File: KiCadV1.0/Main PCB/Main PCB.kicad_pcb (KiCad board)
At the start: 2 copper layers, 79 x 74 mm, 7 parts, among them J1 Conn_01x01_Male, J2 Conn_01x01_Male, U1 TM1637, U2 TM1637, U3 TM1637, U4 NEO6M

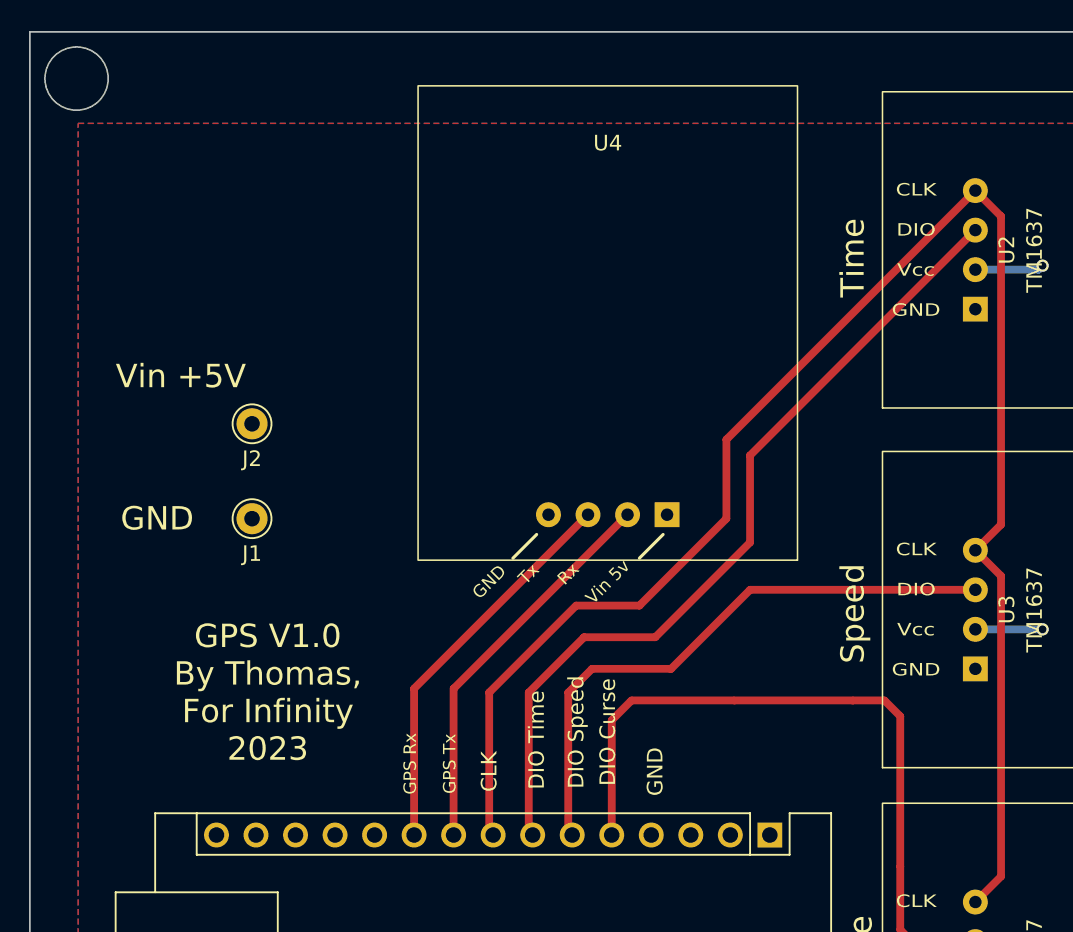
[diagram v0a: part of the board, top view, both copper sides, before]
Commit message: PCB modifs visuelles + Commande
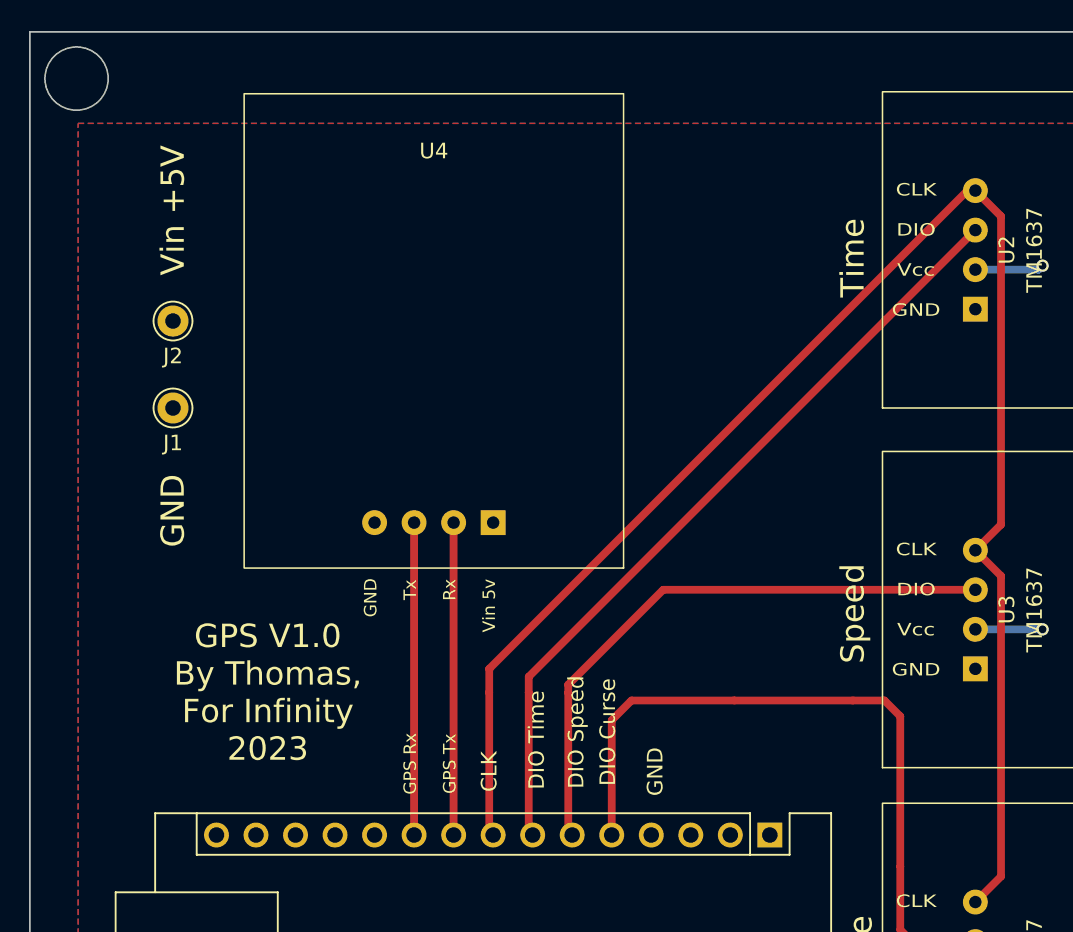
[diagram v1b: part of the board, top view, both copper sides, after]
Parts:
- moved U4 11.2 mm to (61.0, 78.7)
- moved J1 8.74 mm to (44.2, 74.2)
- moved J2 8.33 mm to (44.2, 68.6)
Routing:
- net Net-(U4-Pad2): track 25.2 -> 20.1 mm
- net Net-(U4-Pad3): track 25.2 -> 20.1 mm
- net Net-(A1-Pad7): track 53.5 -> 50.9 mm
- net Net-(U1-Pad4): track 105.3 -> 103.2 mm
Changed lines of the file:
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@@
   )
   (footprint "thomas footprint:NEO6M" (layer "F.Cu")
-    (at 72.136 78.232)
+    (at 60.96 78.74)
     (descr "8-lead though-hole mounted DIP package, row spacing 7.62 mm (300 mils), missing pin 7")
     (tags "THT DIP DIL PDIP 2.54mm 7.62mm 300mil")
@@
   )
   (footprint "Connector_Pin:Pin_D1.0mm_L10.0mm" (layer "F.Cu")
-    (at 49.276 75.184)
+    (at 44.196 68.58)
     (descr "solder Pin_ diameter 1.0mm, hole diameter 1.0mm (press fit), length 10.0mm")
     (tags "solder Pin_ press fit")
@@
   )
   (footprint "Connector_Pin:Pin_D1.0mm_L10.0mm" (layer "F.Cu")
-    (at 49.276 81.28)
+    (at 44.196 74.168)
     (descr "solder Pin_ diameter 1.0mm, hole diameter 1.0mm (press fit), length 10.0mm")
     (tags "solder Pin_ press fit")
@@
   (gr_line (start 111 121) (end 38 121) (layer "F.Paste") (width 0.1))
   (gr_line (start 38 53) (end 111 53) (layer "F.Paste") (width 0.1))
-  (gr_line (start 75.692 82.296) (end 74.168 83.82) (layer "F.SilkS") (width 0.2))
-  (gr_line (start 67.564 82.296) (end 66.04 83.82) (layer "F.SilkS") (width 0.2))
   (gr_circle (center 38 53) (end 40.032 53) (layer "Edge.Cuts") (width 0.1) (fill none))
   (gr_circle (center 111 53) (end 113.032 53) (layer "Edge.Cuts") (width 0.1) (fill none))
@@
     (effects (font (size 1 1) (thickness 0.15)))
   )
-  (gr_text "Vin 5v" (at 72.136 85.344 45) (layer "F.SilkS")
+  (gr_text "Vin 5v" (at 64.516 86.868 90) (layer "F.SilkS")
     (effects (font (size 0.8 0.8) (thickness 0.125)))
   )
@@
     (effects (font (size 1 1) (thickness 0.15)))
   )
-  (gr_text "Vin +5V" (at 44.704 72.136) (layer "F.SilkS")
-    (effects (font (size 1.5 1.5) (thickness 0.3)))
-  )
-  (gr_text "GND" (at 64.516 85.344 45) (layer "F.SilkS")
+  (gr_text "Vin +5V" (at 44.196 61.468 90) (layer "F.SilkS")
+    (effects (font (size 1.5 1.5) (thickness 0.3)))
+  )
+  (gr_text "GND" (at 56.896 86.36 90) (layer "F.SilkS")
     (effects (font (size 0.8 0.8) (thickness 0.125)))
   )
@@
     (effects (font (size 1 1) (thickness 0.15)))
   )
-  (gr_text "Rx" (at 69.596 84.836 45) (layer "F.SilkS")
+  (gr_text "Rx" (at 61.976 85.852 90) (layer "F.SilkS")
     (effects (font (size 0.8 0.8) (thickness 0.125)))
   )
@@
     (effects (font (size 1 1) (thickness 0.15)))
   )
-  (gr_text "GND" (at 43.18 81.28) (layer "F.SilkS")
+  (gr_text "GND" (at 44.196 80.772 90) (layer "F.SilkS")
     (effects (font (size 1.5 1.5) (thickness 0.3)))
   )
@@
     (effects (font (size 0.8 0.8) (thickness 0.125)))
   )
-  (gr_text "Tx" (at 67.056 84.836 45) (layer "F.SilkS")
+  (gr_text "Tx" (at 59.436 85.852 90) (layer "F.SilkS")
     (effects (font (size 0.8 0.8) (thickness 0.125)))
   )
@@
   (segment locked (start 87.884 92.964) (end 89.916 92.964) (width 0.5) (layer "F.Cu") (net 19))
   (segment locked (start 80.264 92.964) (end 87.884 92.964) (width 0.5) (layer "F.Cu") (net 19))
-  (segment (start 95.758 85.852) (end 81.28 85.852) (width 0.5) (layer "F.Cu") (net 20))
-  (segment locked (start 71.12 90.932) (end 69.596 92.456) (width 0.5) (layer "F.Cu") (net 20))
   (segment locked (start 69.596 92.456) (end 69.596 101.356) (width 0.5) (layer "F.Cu") (net 20))
-  (segment (start 76.2 90.932) (end 71.12 90.932) (width 0.5) (layer "F.Cu") (net 20))
+  (segment (start 95.758 85.852) (end 75.692 85.852) (width 0.5) (layer "F.Cu") (net 20))
+  (segment (start 69.596 91.948) (end 69.596 92.456) (width 0.5) (layer "F.Cu") (net 20))
+  (segment (start 75.692 85.852) (end 69.596 91.948) (width 0.5) (layer "F.Cu") (net 20))
   (segment (start 69.596 101.356) (end 69.85 101.61) (width 0.5) (layer "F.Cu") (net 20))
-  (segment (start 81.28 85.852) (end 76.2 90.932) (width 0.5) (layer "F.Cu") (net 20))
-  (segment (start 95.758 62.738) (end 81.28 77.216) (width 0.5) (layer "F.Cu") (net 21))
-  (segment (start 70.612 88.9) (end 67.056 92.456) (width 0.5) (layer "F.Cu") (net 21))
   (segment locked (start 67.056 92.456) (end 67.056 101.356) (width 0.5) (layer "F.Cu") (net 21))
-  (segment (start 75.184 88.9) (end 70.612 88.9) (width 0.5) (layer "F.Cu") (net 21))
+  (segment (start 67.056 91.44) (end 67.056 92.456) (width 0.5) (layer "F.Cu") (net 21))
+  (segment (start 95.758 62.738) (end 67.056 91.44) (width 0.5) (layer "F.Cu") (net 21))
   (segment (start 67.056 101.356) (end 67.31 101.61) (width 0.5) (layer "F.Cu") (net 21))
-  (segment (start 81.28 82.804) (end 75.184 88.9) (width 0.5) (layer "F.Cu") (net 21))
-  (segment (start 81.28 77.216) (end 81.28 82.804) (width 0.5) (layer "F.Cu") (net 21))
-  (segment (start 62.23 92.202) (end 62.23 101.61) (width 0.5) (layer "F.Cu") (net 22))
-  (segment (start 73.406 81.026) (end 62.23 92.202) (width 0.5) (layer "F.Cu") (net 22))
-  (segment (start 70.866 81.026) (end 59.69 92.202) (width 0.5) (layer "F.Cu") (net 23))
-  (segment (start 59.69 92.202) (end 59.69 101.61) (width 0.5) (layer "F.Cu") (net 23))
-  (segment (start 79.756 76.2) (end 79.756 81.28) (width 0.5) (layer "F.Cu") (net 28))
+  (segment (start 62.23 81.534) (end 62.23 101.61) (width 0.5) (layer "F.Cu") (net 22))
+  (segment (start 59.69 81.534) (end 59.69 101.61) (width 0.5) (layer "F.Cu") (net 23))
   (segment (start 97.408001 81.661999) (end 95.758 83.312) (width 0.5) (layer "F.Cu") (net 28))
   (segment (start 95.758 83.312) (end 97.408001 84.962001) (width 0.5) (layer "F.Cu") (net 28))
-  (segment (start 95.758 60.198) (end 79.756 76.2) (width 0.5) (layer "F.Cu") (net 28))
+  (segment (start 95.758 60.198) (end 95.25 60.198) (width 0.5) (layer "F.Cu") (net 28))
+  (segment (start 95.25 60.198) (end 64.516 90.932) (width 0.5) (layer "F.Cu") (net 28))
   (segment (start 97.408001 84.962001) (end 97.408001 104.267999) (width 0.5) (layer "F.Cu") (net 28))
+  (segment (start 64.516 90.932) (end 64.516 92.456) (width 0.5) (layer "F.Cu") (net 28))
   (segment (start 64.516 101.356) (end 64.77 101.61) (width 0.5) (layer "F.Cu") (net 28))
   (segment (start 95.758 60.198) (end 97.408001 61.848001) (width 0.5) (layer "F.Cu") (net 28))
   (segment (start 97.408001 61.848001) (end 97.408001 81.661999) (width 0.5) (layer "F.Cu") (net 28))
   (segment locked (start 64.516 92.456) (end 64.516 101.356) (width 0.5) (layer "F.Cu") (net 28))
-  (segment (start 70.104 86.868) (end 64.516 92.456) (width 0.5) (layer "F.Cu") (net 28))
-  (segment (start 79.756 81.28) (end 74.168 86.868) (width 0.5) (layer "F.Cu") (net 28))
   (segment (start 97.408001 104.267999) (end 95.758 105.918) (width 0.5) (layer "F.Cu") (net 28))
-  (segment (start 74.168 86.868) (end 70.104 86.868) (width 0.5) (layer "F.Cu") (net 28))
   (zone (net 17) (net_name "Vin5v") (layer "F.Cu") (hatch edge 0.508)
     (connect_pads (clearance 0.508))

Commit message: kicad V2 en cours
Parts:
- U1, U2, U3: footprint thomas footprint:TM1637 -> thomas footprint:TM1637 V2 couchée
- moved J1 126.5 mm to (167.6, 101.6), turned to -90 degrees
- moved J2 121.4 mm to (161.1, 101.6), turned to -90 degrees
- moved U4 112.4 mm to (173.4, 78.7), turned to -90 degrees
- moved A1 87.0 mm to (154.9, 53.3), turned to 90 degrees
- moved U2 45.1 mm to (143.4, 59.6), turned to 90 degrees
- moved U3 44.9 mm to (143.4, 85.0), turned to 90 degrees
- moved U1 44.9 mm to (143.4, 110.4), turned to 90 degrees
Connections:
- A1 pad 27: unconnected-(A1-Pad27) -> Vin5v
- A1 pad 30: Vin5v -> unconnected-(A1-VIN-Pad30)
- A1 pad 5: Net-(U1-Pad3) -> Net-(A1-D2)
- A1 pad 7: Net-(A1-Pad7) -> Net-(A1-D4)
- U1 pad 3: Net-(U1-Pad3) -> Net-(A1-D4)
- U2 pad 3: Net-(A1-Pad7) -> Net-(A1-D2)
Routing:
- net GND: track 0.00 -> 118.2 mm
- net Net-(A1-D4): track 0.00 -> 57.2 mm
- net Vin5v: track 8.74 -> 64.3 mm, vias 2 -> 0
- net Net-(A1-Pad7): track 50.9 -> 0.00 mm
- net Net-(U1-Pad3): track 45.7 -> 0.00 mm
- net Net-(A1-D2): track 0.00 -> 34.1 mm
- net Net-(A1-D5): track 103.2 -> 89.1 mm
- net Net-(A1-D6): track 20.1 -> 30.3 mm
- net Net-(A1-D7): track 20.1 -> 27.7 mm
- net Net-(A1-D3): track 38.5 -> 34.6 mm
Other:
- board size 79 x 74 mm -> 254.3 x 157.8 mm
- board text added: "GPS V2.0 By Thomas, For Infinity 2023"
- board text removed: "GPS V1.0 By Thomas, For Infinity 2023"
